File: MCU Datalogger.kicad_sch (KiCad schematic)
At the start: 0 parts

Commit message: Setup of EEschema for new project
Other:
- title: (none) -> ${project_name}
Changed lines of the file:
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@@
 	(generator_version "10.0")
 	(paper "A4")
+	(title_block
+		(title "${project_name}")
+		(date "2026-09-06")
+		(rev "1")
+	)
 	(sheet_instances
 		(path "/"

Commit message: added RISC microcontroller and timer
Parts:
- added BT1: Battery, Package_DFN_QFN:QFN-40-1EP_6x6mm_P0.5mm_EP4.6x4.6mm, symbol Device:Battery
- added C1, C2, C3, C4: C, symbol Device:C
- added C5: C_Polarized, symbol Device:C_Polarized
- added D1, D2: LED, LED_SMD:LED_Cree-XHP50_3V_HighDensity, symbol Device:LED
- added H1, H2, H3, H4: MountingHole, Module:Maple_Mini, symbol Mechanical:MountingHole
- added R1, R2, R3, R4, R5, R6, R7: R, symbol Device:R
- added U1: 24LC1025, Package_SO:SOIC-8_3.9x4.9mm_P1.27mm, symbol Memory_EEPROM:24LC1025
- added U2: 24LC1025, symbol Memory_EEPROM:24LC1025
- added U3: DS1337S+T&R, 21-0041B_8_MXM, symbol 2026-09-06_18-30-11:DS1337S+T&R
- added U4: ATMEGA328P-AU, TQFP32_32A_MCH, symbol 2026-09-06_18-41-55:ATMEGA328P-AU
- added Y1, Y2: Crystal, symbol Device:Crystal
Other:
- company: (none) -> N/A

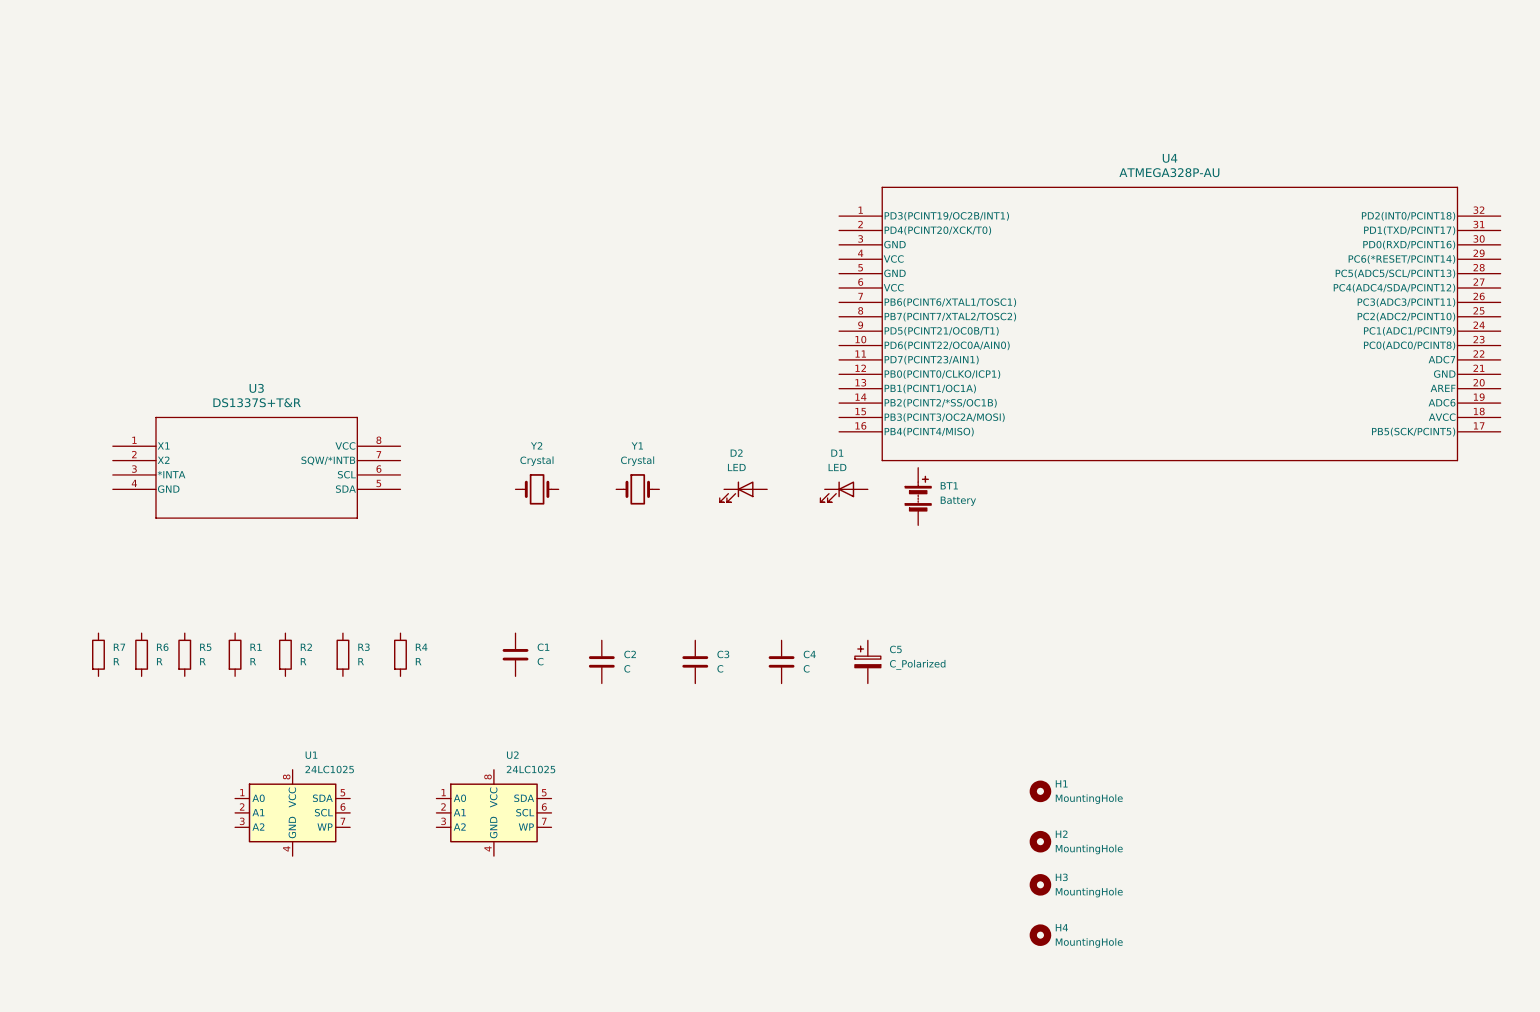
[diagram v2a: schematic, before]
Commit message: made a new connector sheet with components
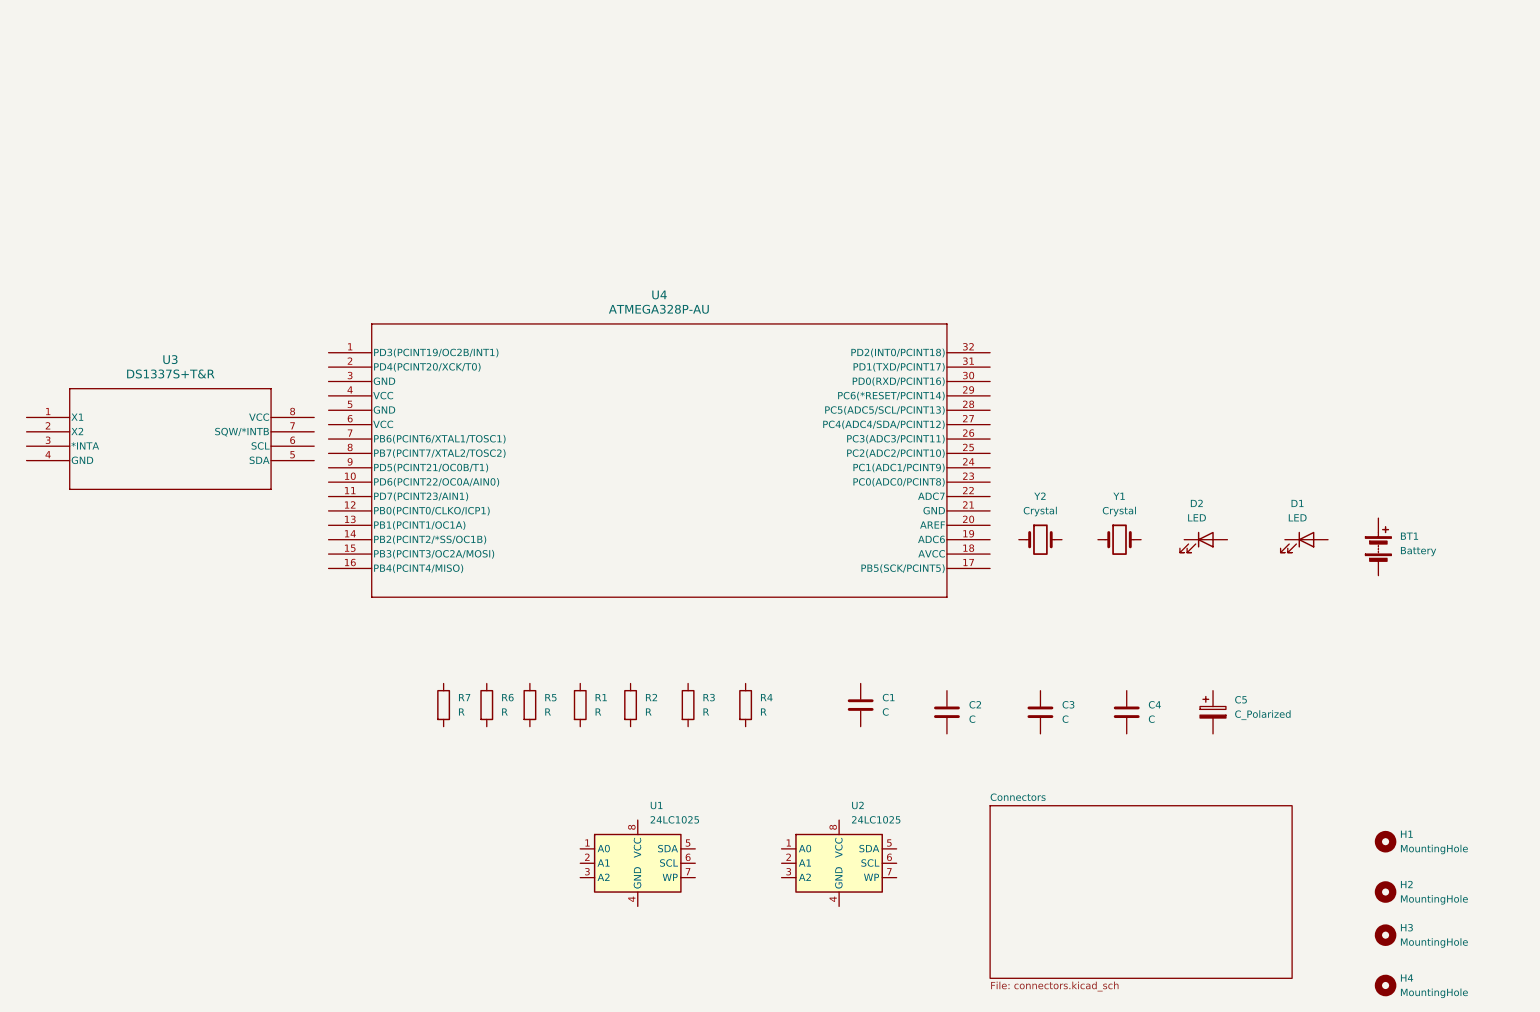
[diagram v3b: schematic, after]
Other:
- added sheet Connectors (connectors.kicad_sch)
- moved on the sheet: BT1, C1, C2, C3, C4, C5, D1, D2, H1, H2, H3, H4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

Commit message: Changed Locations of Symbols
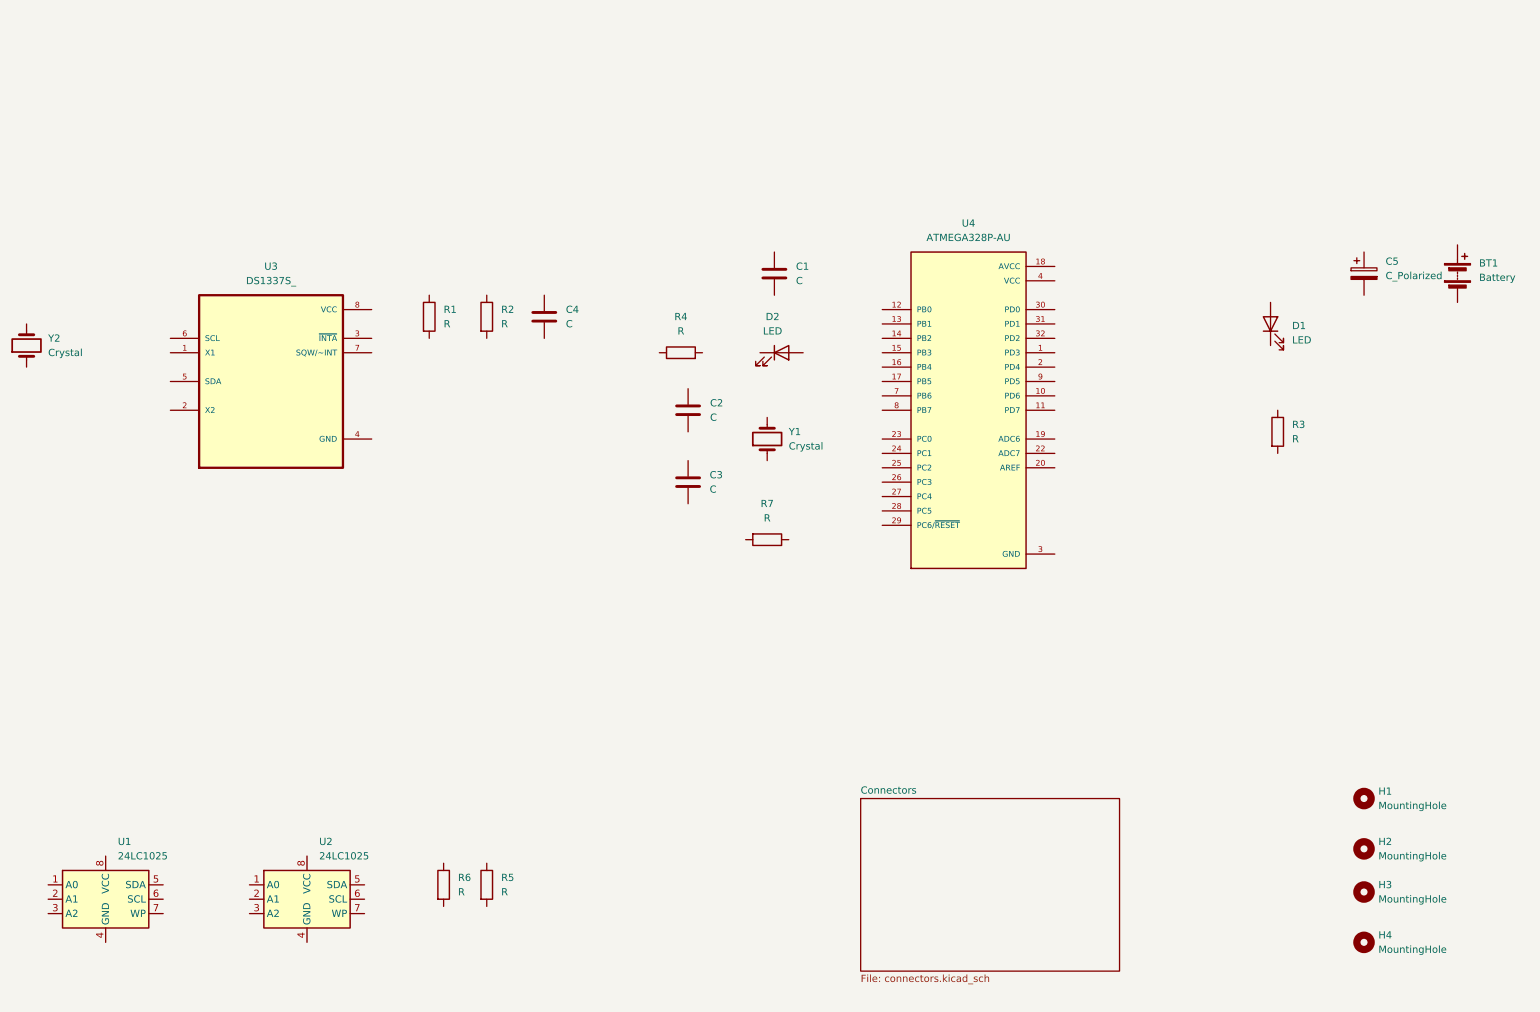
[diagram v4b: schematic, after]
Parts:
- removed U3: DS1337S+T&R, 21-0041B_8_MXM, symbol 2026-09-06_18-30-11:DS1337S+T&R
- removed U4: ATMEGA328P-AU, TQFP32_32A_MCH, symbol 2026-09-06_18-41-55:ATMEGA328P-AU
- added U3: DS1337S_, DS1337S_:SOIC127P600X175-8N, symbol DS1337S_:DS1337S_
- added U4: ATMEGA328P-AU, ATMEGA328P-AU:QFP80P900X900X120-32N, symbol ATMEGA328P-AU:ATMEGA328P-AU
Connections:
- new net GND: U4.21 (GND), U4.3 (GND), U4.5 (GND)
- new net VCC: U4.4 (VCC), U4.6 (VCC)
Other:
- moved on the sheet: BT1, C1, C2, C3, C4, C5, D1, D2, H1, H2, H3, H4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

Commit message: Components Value Added
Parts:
- C1, C4: value C -> 0.1uF
- C2, C3: value C -> 22pF
- C5: value C_Polarized -> 100nF
- R1, R2, R7: value R -> 10K
- R3, R4: value R -> 330
- R5, R6: value R -> 4.7K
- Y1: value Crystal -> 16 MHz
- Y2: value Crystal -> 32.768 kHZ
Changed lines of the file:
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@@
 			)
 		)
-		(property "Value" "Crystal"
+		(property "Value" "32.768 kHZ"
 			(at 22.86 46.9899 90)
 			(show_name no)
@@
 			(at 19.05 45.72 0)
 			(hide yes)
+			(show_name no)
+			(do_not_autoplace no)
+			(effects
+				(font
+					(size 1.27 1.27)
+				)
+			)
+		)
+		(property "Purpose" ""
+			(at 19.05 45.72 0)
 			(show_name no)
 			(do_not_autoplace no)
@@
 			)
 		)
-		(property "Value" "R"
+		(property "Value" "10K"
 			(at 102.87 41.9099 0)
 			(show_name no)
@@
 			(at 100.33 40.64 0)
 			(hide yes)
+			(show_name no)
+			(do_not_autoplace no)
+			(effects
+				(font
+					(size 1.27 1.27)
+				)
+			)
+		)
+		(property "Purpose" ""
+			(at 100.33 40.64 0)
 			(show_name no)
 			(do_not_autoplace no)
@@
 			)
 		)
-		(property "Value" "C"
+		(property "Value" "0.1uF"
 			(at 114.3 41.9099 0)
 			(show_name no)
@@
 			(at 110.49 40.64 0)
 			(hide yes)
+			(show_name no)
+			(do_not_autoplace no)
+			(effects
+				(font
+					(size 1.27 1.27)
+				)
+			)
+		)
+		(property "Purpose" ""
+			(at 110.49 40.64 0)
 			(show_name no)
 			(do_not_autoplace no)
@@
 			)
 		)
-		(property "Value" "R"
+		(property "Value" "10K"
 			(at 92.71 41.9099 0)
 			(show_name no)
@@
 			(at 90.17 40.64 0)
 			(hide yes)
+			(show_name no)
+			(do_not_autoplace no)
+			(effects
+				(font
+					(size 1.27 1.27)
+				)
+			)
+		)
+		(property "Purpose" ""
+			(at 90.17 40.64 0)
 			(show_name no)
 			(do_not_autoplace no)
@@
 			)
 		)
-		(property "Value" "R"
+		(property "Value" "4.7K"
 			(at 102.87 142.2399 0)
 			(show_name no)
@@
 			(at 100.33 140.97 0)
 			(hide yes)
+			(show_name no)
+			(do_not_autoplace no)
+			(effects
+				(font
+					(size 1.27 1.27)
+				)
+			)
+		)
+		(property "Purpose" ""
+			(at 100.33 140.97 0)
 			(show_name no)
 			(do_not_autoplace no)
@@
 			)
 		)
-		(property "Value" "C_Polarized"
+		(property "Value" "100nF"
 			(at 259.08 33.4009 0)
 			(show_name no)
@@
 			(at 255.27 33.02 0)
 			(hide yes)
+			(show_name no)
+			(do_not_autoplace no)
+			(effects
+				(font
+					(size 1.27 1.27)
+				)
+			)
+		)
+		(property "Purpose" ""
+			(at 255.27 33.02 0)
 			(show_name no)
 			(do_not_autoplace no)
@@
 			)
 		)
-		(property "Value" "C"
+		(property "Value" "0.1uF"
 			(at 154.94 34.2899 0)
 			(show_name no)
@@
 			(at 151.13 33.02 0)
 			(hide yes)
+			(show_name no)
+			(do_not_autoplace no)
+			(effects
+				(font
+					(size 1.27 1.27)
+				)
+			)
+		)
+		(property "Purpose" ""
+			(at 151.13 33.02 0)
 			(show_name no)
 			(do_not_autoplace no)
@@
 			)
 		)
-		(property "Value" "R"
+		(property "Value" "10K"
 			(at 149.86 76.2 90)
 			(show_name no)
@@
 			(at 149.86 80.01 0)
 			(hide yes)
+			(show_name no)
+			(do_not_autoplace no)
+			(effects
+				(font
+					(size 1.27 1.27)
+				)
+			)
+		)
+		(property "Purpose" ""
+			(at 149.86 80.01 0)
 			(show_name no)
 			(do_not_autoplace no)
@@
 			)
 		)
-		(property "Value" "Crystal"
+		(property "Value" "16 MHz"
 			(at 153.67 63.4999 90)
 			(show_name no)
@@
 			(at 149.86 62.23 0)
 			(hide yes)
+			(show_name no)
+			(do_not_autoplace no)
+			(effects
+				(font
+					(size 1.27 1.27)
+				)
+			)
+		)
+		(property "Purpose" ""
+			(at 149.86 62.23 0)
 			(show_name no)
 			(do_not_autoplace no)
@@
 			)
 		)
-		(property "Value" "C"
+		(property "Value" "22pF"
 			(at 139.7 71.1199 0)
 			(show_name no)
@@
 			(at 135.89 69.85 0)
 			(hide yes)
+			(show_name no)
+			(do_not_autoplace no)
+			(effects
+				(font
+					(size 1.27 1.27)
+				)
+			)
+		)
+		(property "Purpose" ""
+			(at 135.89 69.85 0)
 			(show_name no)
 			(do_not_autoplace no)
@@
 			)
 		)
-		(property "Value" "R"
+		(property "Value" "330"
 			(at 242.57 62.2299 0)
 			(show_name no)
@@
 			(at 240.03 60.96 0)
 			(hide yes)
+			(show_name no)
+			(do_not_autoplace no)
+			(effects
+				(font
+					(size 1.27 1.27)
+				)
+			)
+		)
+		(property "Purpose" ""
+			(at 240.03 60.96 0)
 			(show_name no)
 			(do_not_autoplace no)
@@
 			)
 		)
-		(property "Value" "C"
+		(property "Value" "22pF"
 			(at 139.7676 58.4199 0)
 			(show_name no)
@@
 			(at 135.89 57.15 0)
 			(hide yes)
+			(show_name no)
+			(do_not_autoplace no)
+			(effects
+				(font
+					(size 1.27 1.27)
+				)
+			)
+		)
+		(property "Purpose" ""
+			(at 135.89 57.15 0)
 			(show_name no)
 			(do_not_autoplace no)
@@
 			)
 		)
-		(property "Value" "R"
+		(property "Value" "330"
 			(at 134.62 43.18 90)
 			(show_name no)
@@
 			(at 134.62 46.99 0)
 			(hide yes)
+			(show_name no)
+			(do_not_autoplace no)
+			(effects
+				(font
+					(size 1.27 1.27)
+				)
+			)
+		)
+		(property "Purpose" ""
+			(at 134.62 46.99 0)
 			(show_name no)
 			(do_not_autoplace no)
@@
 			)
 		)
-		(property "Value" "R"
+		(property "Value" "4.7K"
 			(at 95.25 142.2399 0)
 			(show_name no)
@@
 			(show_name no)
 			(do_not_autoplace no)
+			(effects
+				(font
+					(size 1.27 1.27)
+				)
+			)
+		)
+		(property "Purpose" ""
+			(at 92.71 140.97 0)
+			(show_name no)
+			(do_not_autoplace no)

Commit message: Completed symbols to footprint association
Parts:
- BT1: footprint Package_DFN_QFN:QFN-40-1EP_6x6mm_P0.5mm_EP4.6x4.6mm -> Connector_PinHeader_2.54mm:PinHeader_1x02_P2.54mm_Vertical
- C1, C2, C3, C4, C5: footprint (none) -> Capacitor_SMD:C_0805_2012Metric
- D1, D2: footprint LED_SMD:LED_Cree-XHP50_3V_HighDensity -> LED_SMD:LED_0805_2012Metric
- H1, H2, H3, H4: footprint Module:Maple_Mini -> MountingHole:MountingHole_2.1mm
- R1, R2, R3, R4, R5, R6, R7: footprint (none) -> Resistor_SMD:R_0805_2012Metric
- U1: footprint Package_SO:SOIC-8_3.9x4.9mm_P1.27mm -> Package_SO:SOIC-8_5.3x5.3mm_P1.27mm
- U2: footprint (none) -> Package_SO:SOIC-8_5.3x5.3mm_P1.27mm
- Y1, Y2: footprint (none) -> Crystal:Crystal_SMD_5032-2Pin_5.0x3.2mm_HandSoldering
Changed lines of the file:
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@@
 			)
 		)
-		(property "Footprint" ""
+		(property "Footprint" "Crystal:Crystal_SMD_5032-2Pin_5.0x3.2mm_HandSoldering"
 			(at 19.05 45.72 0)
 			(hide yes)
@@
 			)
 		)
-		(property "Footprint" ""
+		(property "Footprint" "Resistor_SMD:R_0805_2012Metric"
 			(at 98.552 40.64 90)
 			(hide yes)
@@
 			)
 		)
-		(property "Footprint" ""
+		(property "Footprint" "Capacitor_SMD:C_0805_2012Metric"
 			(at 111.4552 44.45 0)
 			(hide yes)
@@
 			)
 		)
-		(property "Footprint" ""
+		(property "Footprint" "Resistor_SMD:R_0805_2012Metric"
 			(at 88.392 40.64 90)
 			(hide yes)
@@
 			)
 		)
-		(property "Footprint" ""
+		(property "Footprint" "Resistor_SMD:R_0805_2012Metric"
 			(at 98.552 140.97 90)
 			(hide yes)
@@
 			)
 		)
-		(property "Footprint" ""
+		(property "Footprint" "Capacitor_SMD:C_0805_2012Metric"
 			(at 256.2352 36.83 0)
 			(hide yes)
@@
 			)
 		)
-		(property "Footprint" ""
+		(property "Footprint" "Capacitor_SMD:C_0805_2012Metric"
 			(at 152.0952 36.83 0)
 			(hide yes)
@@
 			)
 		)
-		(property "Footprint" ""
+		(property "Footprint" "Resistor_SMD:R_0805_2012Metric"
 			(at 149.86 78.232 90)
 			(hide yes)
@@
 			)
 		)
-		(property "Footprint" "Package_SO:SOIC-8_3.9x4.9mm_P1.27mm"
+		(property "Footprint" "Package_SO:SOIC-8_5.3x5.3mm_P1.27mm"
 			(at 33.02 143.51 0)
 			(hide yes)
@@
 			)
 		)
-		(property "Footprint" "Module:Maple_Mini"
+		(property "Footprint" "MountingHole:MountingHole_2.1mm"
 			(at 255.27 125.73 0)
 			(hide yes)
@@
 			)
 		)
-		(property "Footprint" ""
+		(property "Footprint" "Crystal:Crystal_SMD_5032-2Pin_5.0x3.2mm_HandSoldering"
 			(at 149.86 62.23 0)
 			(hide yes)
@@
 			)
 		)
-		(property "Footprint" "LED_SMD:LED_Cree-XHP50_3V_HighDensity"
+		(property "Footprint" "LED_SMD:LED_0805_2012Metric"
 			(at 152.4 46.99 0)
 			(hide yes)
@@
 			)
 		)
-		(property "Footprint" ""
+		(property "Footprint" "Capacitor_SMD:C_0805_2012Metric"
 			(at 136.8552 73.66 0)
 			(hide yes)
@@
 			)
 		)
-		(property "Footprint" "Module:Maple_Mini"
+		(property "Footprint" "MountingHole:MountingHole_2.1mm"
 			(at 255.27 151.13 0)
 			(hide yes)
@@
 			)
 		)
-		(property "Footprint" ""
+		(property "Footprint" "Resistor_SMD:R_0805_2012Metric"
 			(at 238.252 60.96 90)
 			(hide yes)
@@
 			)
 		)
-		(property "Footprint" "LED_SMD:LED_Cree-XHP50_3V_HighDensity"
+		(property "Footprint" "LED_SMD:LED_0805_2012Metric"
 			(at 238.76 41.91 0)
 			(hide yes)
@@
 			)
 		)
-		(property "Footprint" ""
+		(property "Footprint" "Capacitor_SMD:C_0805_2012Metric"
 			(at 136.8552 60.96 0)
 			(hide yes)
@@
 			)
 		)
-		(property "Footprint" ""
+		(property "Footprint" "Resistor_SMD:R_0805_2012Metric"
 			(at 134.62 48.768 90)
 			(hide yes)
@@
 			)
 		)
-		(property "Footprint" "Module:Maple_Mini"
+		(property "Footprint" "MountingHole:MountingHole_2.1mm"
 			(at 255.27 134.62 0)
 			(hide yes)
@@
 			)
 		)
-		(property "Footprint" "Module:Maple_Mini"
+		(property "Footprint" "MountingHole:MountingHole_2.1mm"
 			(at 255.27 142.24 0)
 			(hide yes)
@@
 			)
 		)
-		(property "Footprint" ""
+		(property "Footprint" "Package_SO:SOIC-8_5.3x5.3mm_P1.27mm"
 			(at 68.58 143.51 0)
 			(hide yes)
@@
 			)
 		)
-		(property "Footprint" ""
+		(property "Footprint" "Resistor_SMD:R_0805_2012Metric"
 			(at 90.932 140.97 90)
 			(hide yes)
@@
 			)
 		)
-		(property "Footprint" "Package_DFN_QFN:QFN-40-1EP_6x6mm_P0.5mm_EP4.6x4.6mm"
+		(property "Footprint" "Connector_PinHeader_2.54mm:PinHeader_1x02_P2.54mm_Vertical"
 			(at 271.78 31.496 90)
 			(hide yes)
